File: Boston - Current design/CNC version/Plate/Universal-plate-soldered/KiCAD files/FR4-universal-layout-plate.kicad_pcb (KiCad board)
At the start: 2 copper layers, 397 x 159.9 mm, 16 parts

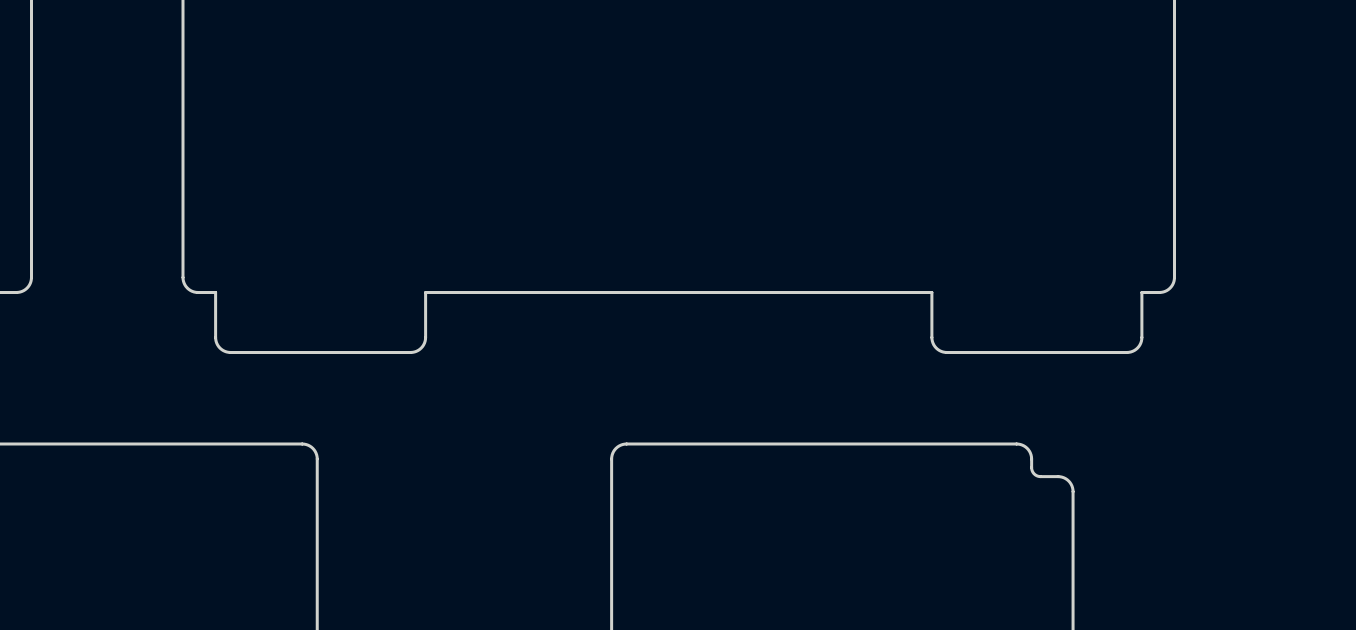
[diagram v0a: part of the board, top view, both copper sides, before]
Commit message: Fixed some sharp corners
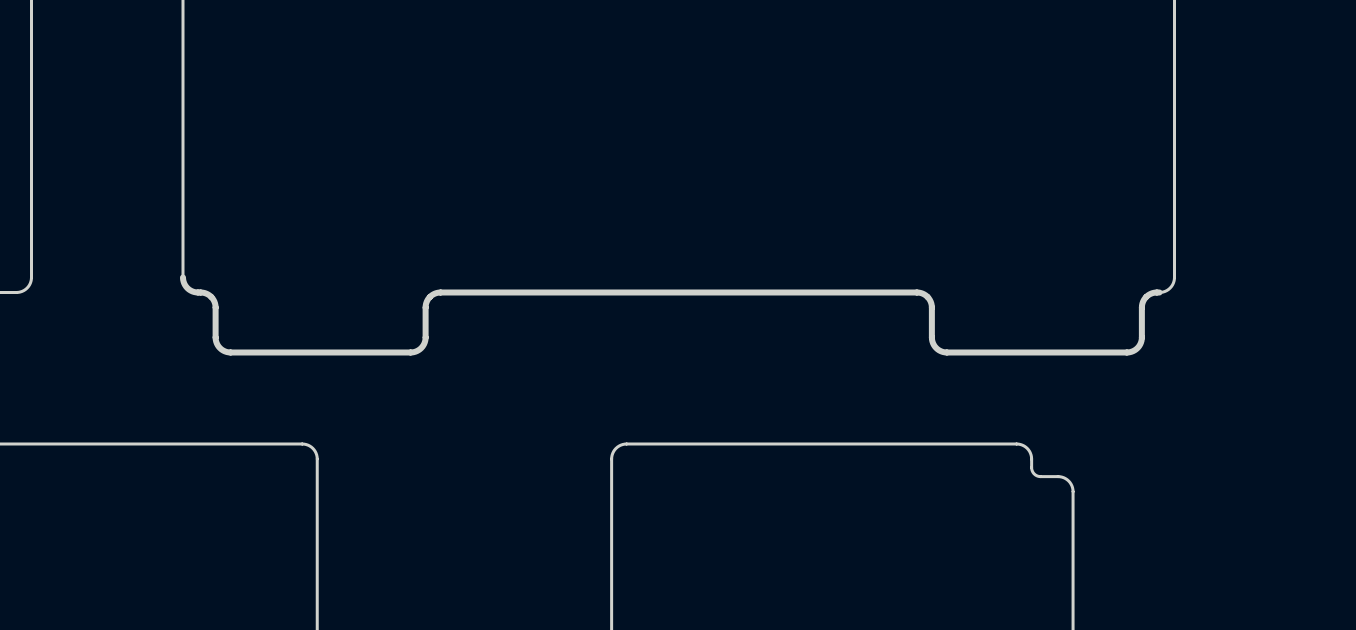
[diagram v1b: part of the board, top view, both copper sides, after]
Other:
- outline, holes or cut-outs redrawn
- board text added: "Boston (Metal Version) - Universal Plate V0.3 - June 27, 2023 Designed by Pylon"
- board text removed: "Boston (Metal Version) - Universal Plate V0.2 - March 7, 2021 Designed by Pylon"
